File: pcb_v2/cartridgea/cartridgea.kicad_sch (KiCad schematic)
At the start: 11 parts, among them J1 cartridge, SW1 ADDR, U1 28C256, U2 28C256, U3 74LS138

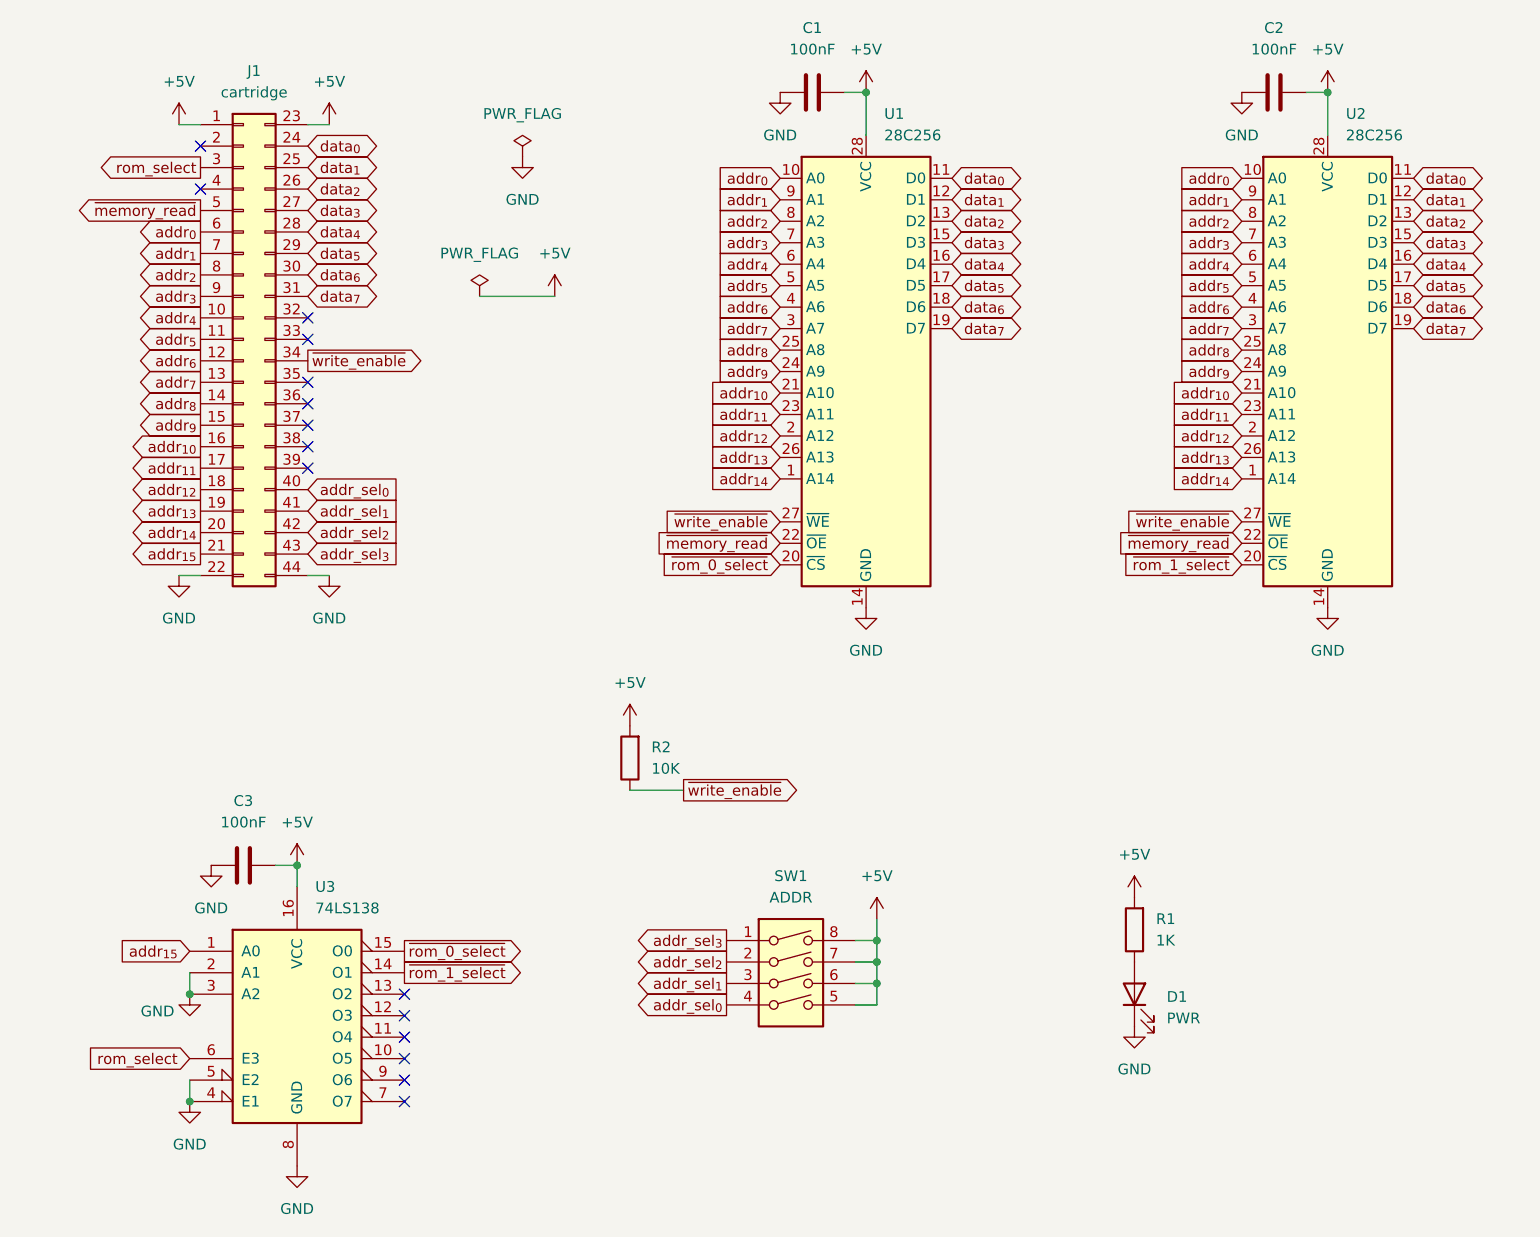
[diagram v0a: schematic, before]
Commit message: seleção de chip de rom feita pela placa de memória; isso reduz[A um chip no cartucho
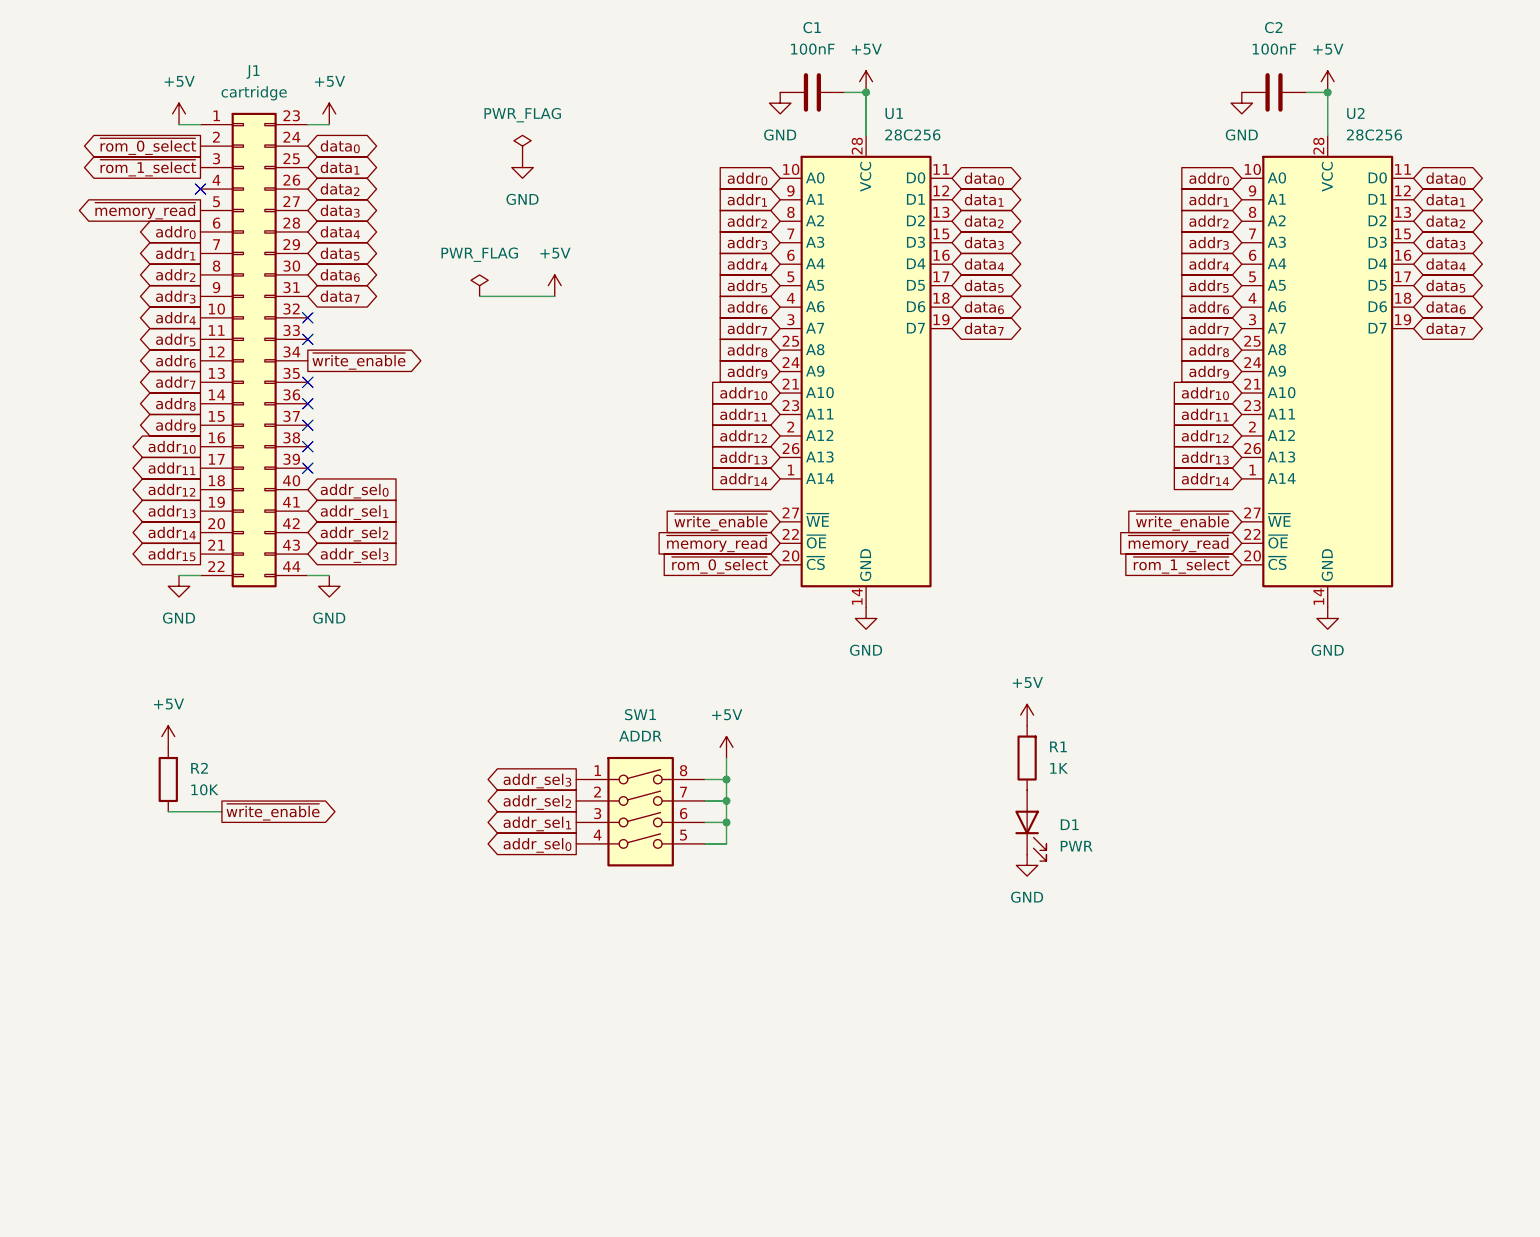
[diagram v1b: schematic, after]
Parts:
- removed C3: 100nF, Capacitor_THT:C_Disc_D5.1mm_W3.2mm_P5.00mm, symbol Device:C
- removed U3: 74LS138, Package_DIP:DIP-16_W7.62mm, symbol 74xx:74LS138
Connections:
- net rom_select is gone; now on net ~{rom_1_select}: J1.3 (Pin_3)
- net ~{rom_0_select}: now also J1.2 (Pin_2)
- no-connect marks 15 -> 8
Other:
- moved on the sheet: D1, R1, R2, SW1
